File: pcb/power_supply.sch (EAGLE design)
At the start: 19 parts, among them J1 10103594-0001LF, U1 RASPBERRY_PI_3_MODEL_B+, U2 LM1085IT-5.0, U3 TI_NATIONAL_SEMICONDUCTOR_LM2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, X1 MKKDS02, X2 MKKDS02, X3 MKKDS02, X4 MKKDS02

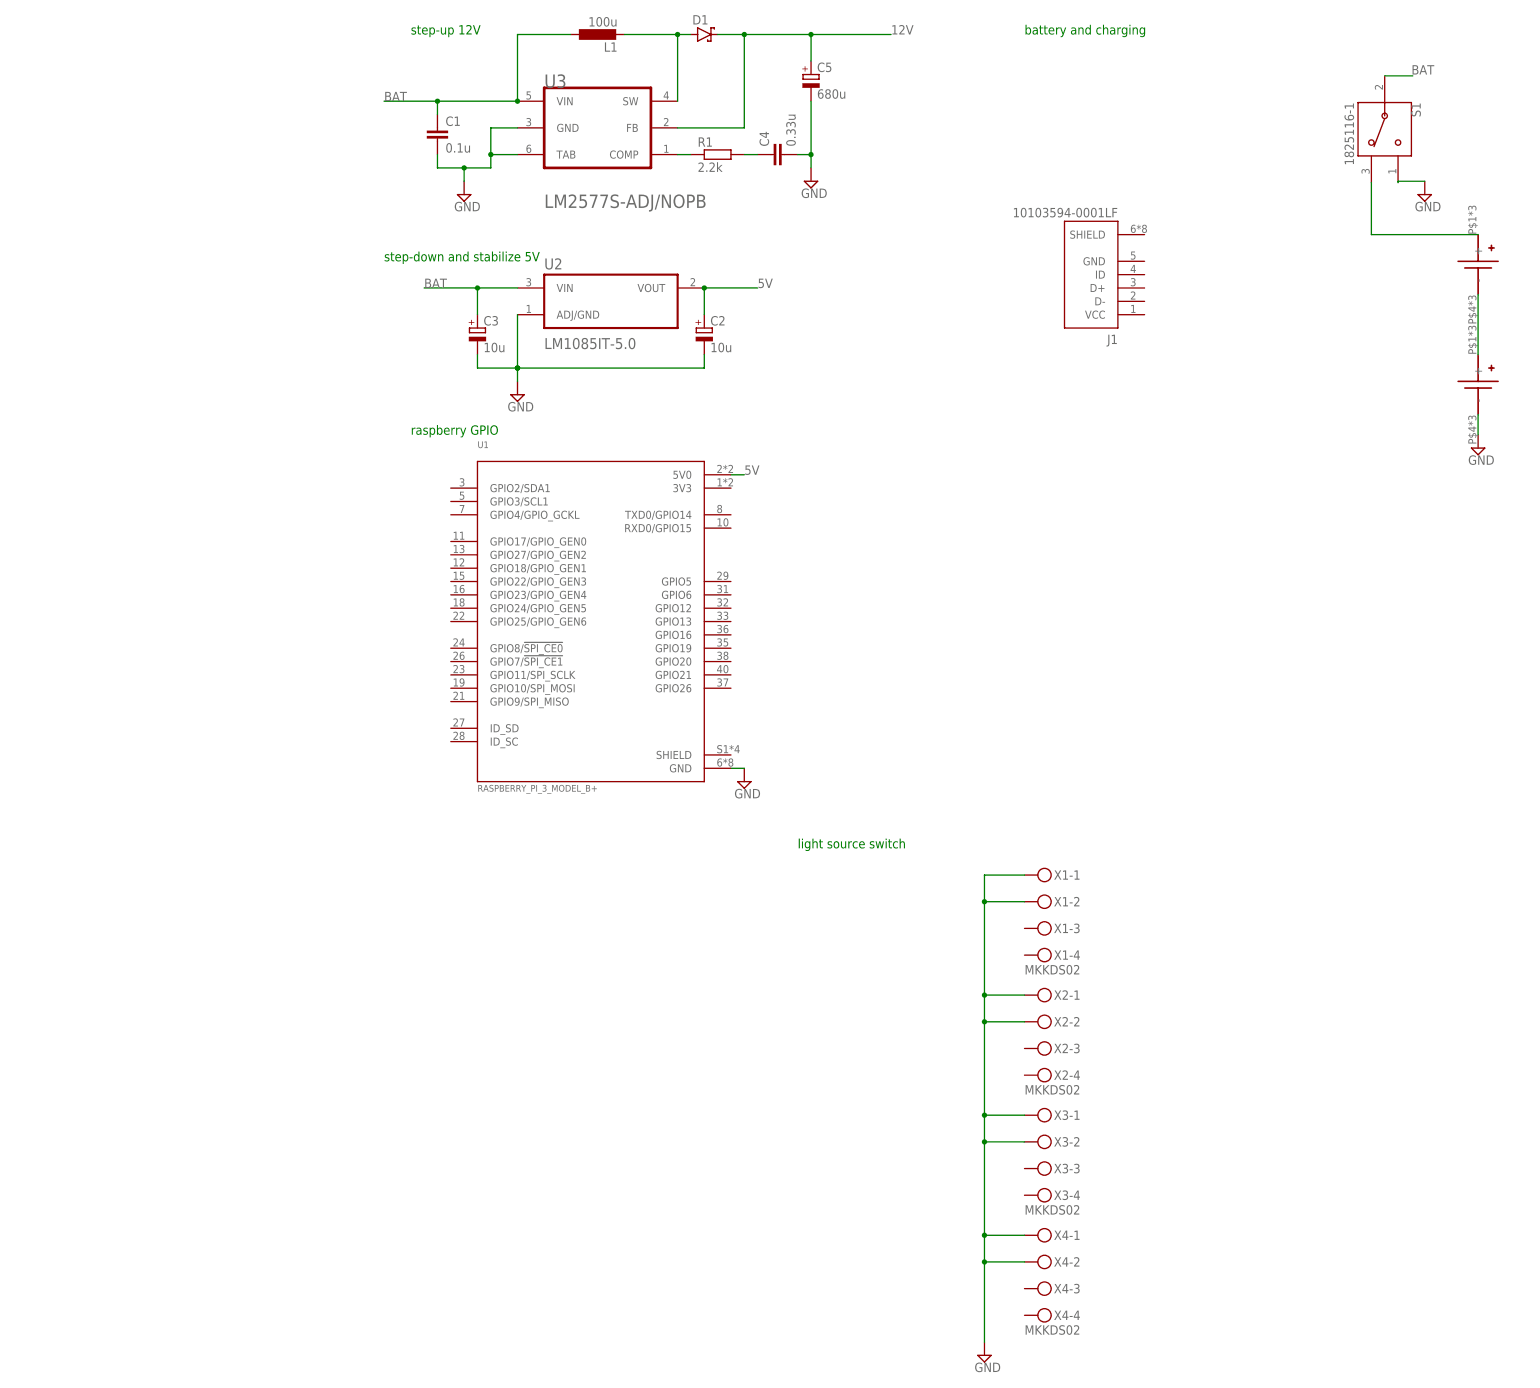
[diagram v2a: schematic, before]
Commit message: pcb - lights switching, battery replacement to 2*6V
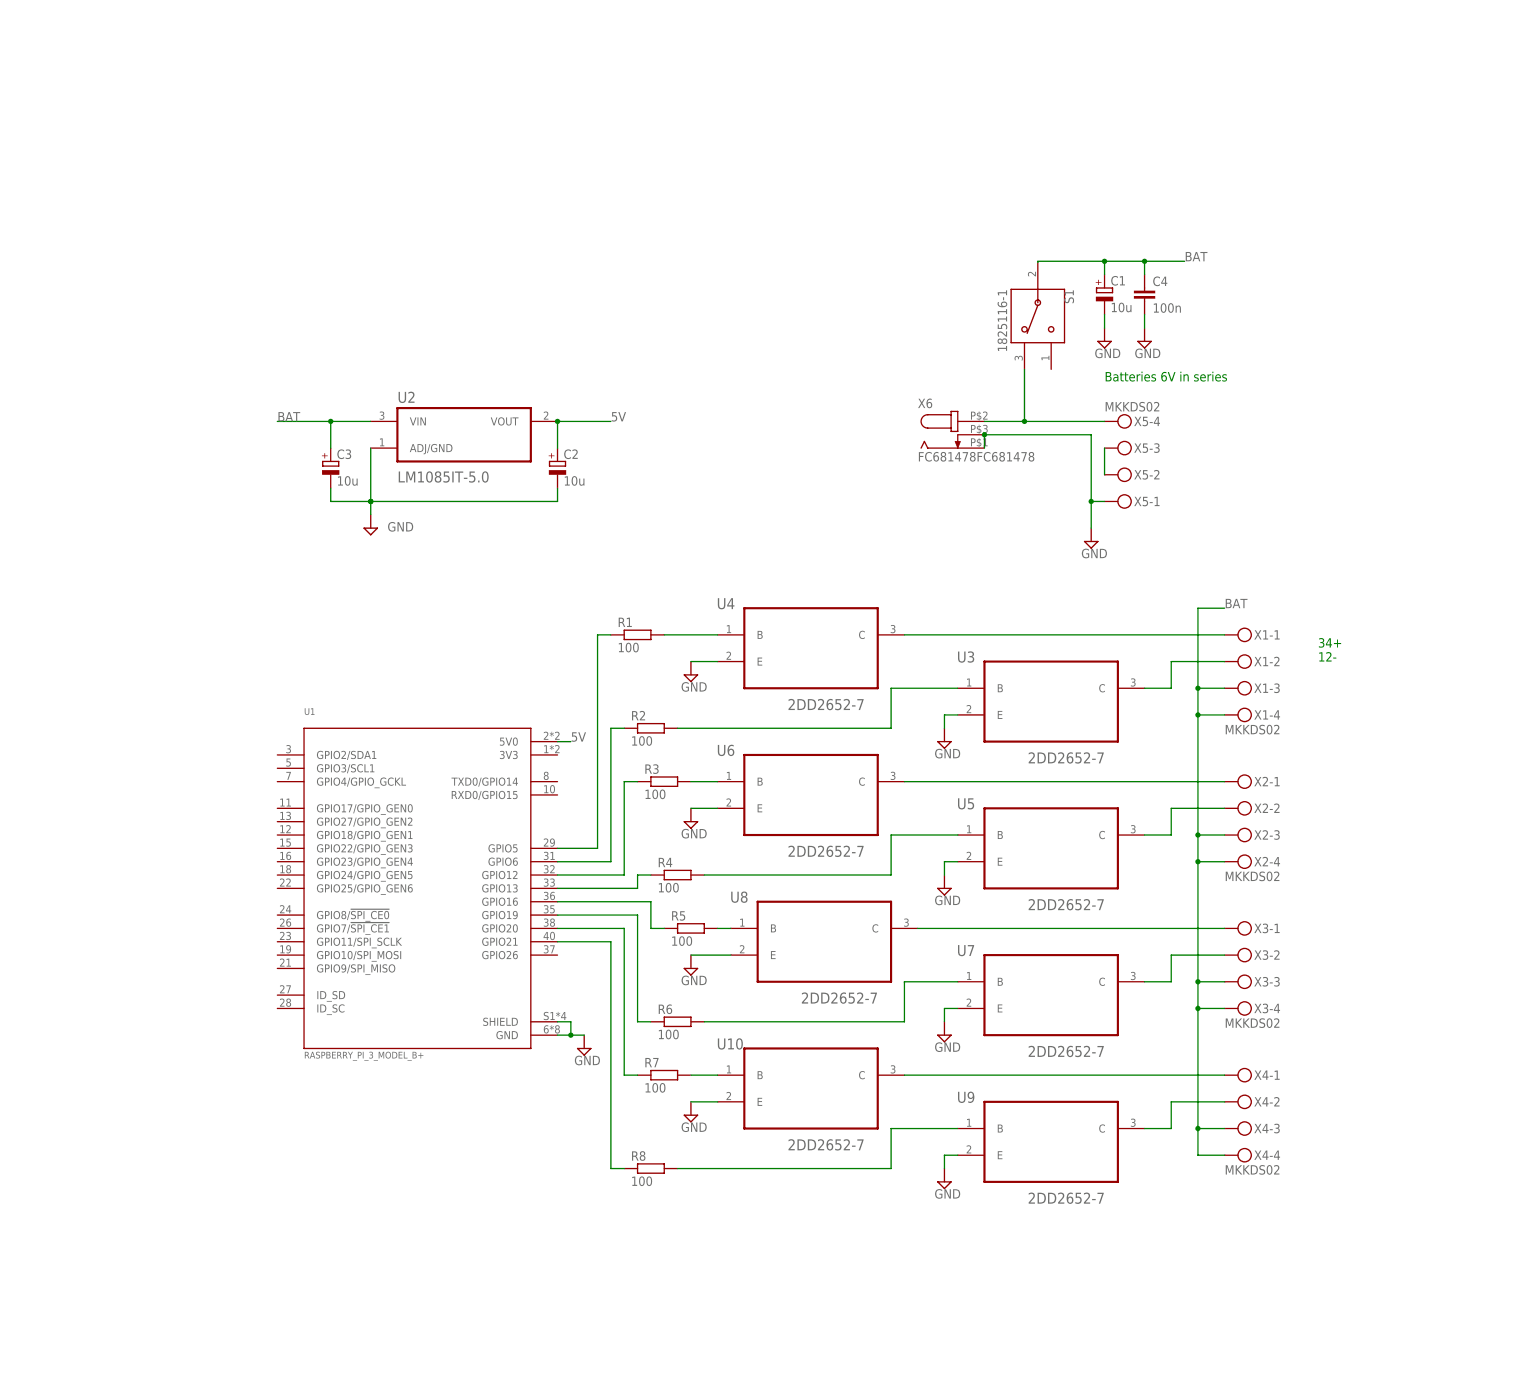
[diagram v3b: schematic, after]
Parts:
- removed C5: 680u, rcl:CPOL-EUSMCB
- removed D1: (no value), diode:SCHOTTKY-DIODEDO35-7
- removed J1: 10103594-0001LF, 10103594-0001LF:10103594-0001LF
- removed L1: 100u, rcl:L-EU0207/5V
- removed U$1, U$2: KEYESTONE_54A_3D, battery-holders:KEYESTONE_54A_3D
- added R2, R3, R4, R5, R6, R7, R8: 100, rcl:R-EU_R0805
- added U10, U4, U5, U6, U7, U8, U9: 2DD2652-7, 2DD2652-7:2DD2652-7
- added X5: MKKDS02, con-phoenix-508:MKKDS02
- added X6: FC681478FC681478, FC681478:FC681478FC681478
- C1: value 0.1u -> 10u; device rcl:C-EUC0805 -> rcl:CPOL-EUSMCB
- C4: value 0.33u -> 100n
- R1: value 2.2k -> 100
- U3: value TI_NATIONAL_SEMICONDUCTOR_LM2577S-ADJ-NOPBTI_NATIONAL_SEMICONDUCTOR_LM2577S-ADJ-NOPB_0_2 -> 2DD2652-7; device LM2577S-ADJ_NOPB:TI_NATIONAL_SEMICONDUCTOR_LM2577S-ADJ-NOPBTI_NATIONAL_SEMICONDUCTOR_LM2577S-ADJ-NOPB_0_2 -> 2DD2652-7:2DD2652-7
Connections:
- removed net 12V: C5.+, D1.C, U3.FB
- new net N$10: U6.C, X2-1.KL
- new net N$11: R4.2, U5.B
- new net N$12: U8.C, X3-1.KL
- new net N$13: U10.C, X4-1.KL
- new net N$14: U5.C, X2-2.KL
- new net N$15: U7.C, X3-2.KL
- new net N$16: U9.C, X4-2.KL
- new net N$17: R3.1, U1.GPIO12
- new net N$18: R7.1, U1.GPIO20
- new net N$19: R5.1, U1.GPIO16
- new net N$20: R6.2, U7.B
- new net N$21: R2.1, U1.GPIO6
- new net N$22: R1.2, U4.B
- new net N$23: R4.1, U1.GPIO13
- new net N$24: R3.2, U6.B
- new net N$25: R8.2, U9.B
- new net N$26: R5.2, U8.B
- new net N$27: R7.2, U10.B
- new net N$6: R2.2, U3.B
- new net N$8: U3.C, X1-2.KL
- new net N$9: R8.1, U1.GPIO21
- net BAT: now also C1.+, C4.1, X1-3.KL, X1-4.KL, X2-3.KL, X2-4.KL, X3-3.KL, X3-4.KL, X4-3.KL, X4-4.KL; no longer C1.1, L1.1, U3.VIN
- net GND: now also C1.-, U1.SHIELD, U10.E, U3.E, U4.E, U5.E, U6.E, U7.E, U8.E, U9.E, X5-1.KL, X6.1, X6.2; no longer C1.2, C5.-, S1.1, U$2.-, U3.GND, U3.TAB, X1-1.KL, X1-2.KL, X2-1.KL, X2-2.KL, X3-1.KL, X3-2.KL, X4-1.KL, X4-2.KL
- net N$1: now also U4.C, X1-1.KL; no longer U$1.-, U$2.+
- net N$3: now also X5-4.KL, X6.3; no longer U$1.+
- net N$4: now also X5-2.KL, X5-3.KL; no longer R1.1, U3.COMP
- net N$5: now also R1.1, U1.GPIO5; no longer D1.A, L1.2, U3.SW
- net N$7: now also R6.1, U1.GPIO19; no longer C4.1, R1.2
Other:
- note added: "34+ 12-"
- note added: "Batteries 6V in series"
- note removed: "battery and charging"
- note removed: "light source switch"
- note removed: "raspberry GPIO"
- note removed: "step-down and stabilize 5V"
- note removed: "step-up 12V"
- moved on the sheet: C2, C3, C4, R1, S1, U1, U2, X1-1, X1-2, X1-3, X1-4, X2-1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

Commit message: Some battery replacement and stuff
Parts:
- removed C3: 10u, rcl:CPOL-EUSMCB
- removed S1: 1825116-1, 1825116-1:1825116-1
- added C5, C6, C7: 10u, rcl:CPOL-EUB/3528-21R
- added R9: (no value), pot:TRIM_EU-CA6V
- added U11: TI_NATIONAL_SEMICONDUCTOR_LM1085IT-12-NOPBTI_NATIONAL_SEMIC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, LM1085IT-12:TI_NATIONAL_SEMICONDUCTOR_LM1085IT-12-NOPBTI_NATIONAL_SEMICONDUCTOR_LM1085IT-12-NOPB_0_0
- added X7: MKDSN1,5/2-5,08, con-phoenix-508:MKDSN1,5/2-5,08
- C1, C2: device rcl:CPOL-EUSMCB -> rcl:CPOL-EUB/3528-21R
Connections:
- new net 12V: C2.+, R9.A, U11.OUT
- new net LIGHTS+: R9.S, X1-3.KL, X1-4.KL, X2-3.KL, X2-4.KL, X3-3.KL, X3-4.KL, X4-3.KL, X4-4.KL
- new net N$28: X7-1.KL
- net 5V: now also C5.+; no longer C2.+
- net BAT: now also C6.+, C7.+, U11.IN, X7-2.KL; no longer C3.+, S1.2, X1-3.KL, X1-4.KL, X2-3.KL, X2-4.KL, X3-3.KL, X3-4.KL, X4-3.KL, X4-4.KL
- net GND: now also C5.-, C6.-, C7.-, U11.GND; no longer C3.-
- net N$3: no longer S1.3
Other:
- note added: "switch"
- moved on the sheet: C1, C2

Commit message: pcb - schematic done for now
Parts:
- removed C5, C6, C7: 10u, rcl:CPOL-EUB/3528-21R
- removed U1: RASPBERRY_PI_3_MODEL_B+, RASPBERRY_PI_3_MODEL_B_:RASPBERRY_PI_3_MODEL_B+
- removed U10, U3, U4, U5, U6, U7, U8, U9: 2DD2652-7, 2DD2652-7:2DD2652-7
- removed U11: TI_NATIONAL_SEMICONDUCTOR_LM1085IT-12-NOPBTI_NATIONAL_SEMIC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, LM1085IT-12:TI_NATIONAL_SEMICONDUCTOR_LM1085IT-12-NOPBTI_NATIONAL_SEMICONDUCTOR_LM1085IT-12-NOPB_0_0
- removed U2: LM1085IT-5.0, LM1085IT-5.0:LM1085IT-5.0
- removed X1, X2, X3, X4, X5: MKKDS02, con-phoenix-508:MKKDS02
- removed X6: FC681478FC681478, FC681478:FC681478FC681478
- removed X7: MKDSN1,5/2-5,08, con-phoenix-508:MKDSN1,5/2-5,08
- added BATTERY1, BATTERY2, SWITCH1: 1751248, con-phoenix-350:1751248
- added C3: 10u, rcl:CPOL-EUB/3528-21R
- added DC_CON: FC681478FC681478, FC681478:FC681478FC681478
- added L1, L2, L3, L4, L5, L6, L7, L8: (no value), con-phoenix-254:MPT2
- added LM1085IT-ADJ_1, LM1085IT-ADJ_2: LM1085IT-ADJ, LM1085IT-ADJ:LM1085IT-ADJ
- added P1: 2k, pot:TRIM_EU-CA6V
- added Q1, Q2, Q3, Q4, Q5, Q6, Q7, Q8: DIODES_FMMT493ATADIODES_FMMT493ATA_0_0, Diodes - FMMT493ATA:DIODES_FMMT493ATADIODES_FMMT493ATA_0_0
- added R10, R12: 120, rcl:R-EU_R0805
- added R11: 200, rcl:R-EU_R0805
- added R13: 39, rcl:R-EU_R0805
- added R14: 10, rcl:R-EU_R0805
- added RASPBERRY: RASPBERRY_PI_3_MODEL_B+, RASPBERRY_PI_3_MODEL_B_:RASPBERRY_PI_3_MODEL_B+
- C4: value 100n -> 10u; device rcl:C-EUC0805 -> rcl:CPOL-EUB/3528-21R
- R9: value (none) -> 120; device pot:TRIM_EU-CA6V -> rcl:R-EU_R0805
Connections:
- removed net 12V: C2.+, R9.A, U11.OUT
- removed net N$28: X7-1.KL
- new net N$2: LM1085IT-ADJ_2.ADJ/GND, R10.1, R11.2
- new net N$29: LM1085IT-ADJ_1.ADJ/GND, P1.S, R9.1
- new net N$30: R11.1, R12.2
- new net N$31: R12.1, R13.2
- new net N$32: R13.1, R14.1
- net 5V: now also C4.+, LM1085IT-ADJ_2.OUT, R10.2, RASPBERRY.5V0; no longer C5.+, U1.5V0, U2.VOUT
- net BAT: now also C3.+, LM1085IT-ADJ_1.IN, LM1085IT-ADJ_2.IN, SWITCH1-2.K; no longer C4.1, C6.+, C7.+, U11.IN, U2.VIN, X7-2.KL
- net GND: now also BATTERY2-2.K, C3.-, C4.-, DC_CON.1, DC_CON.2, P1.A, Q1.E, Q2.E, Q3.E, Q4.E, Q5.E, Q6.E, Q7.E, Q8.E, R14.2, RASPBERRY.GND, RASPBERRY.SHIELD; no longer C4.2, C5.-, C6.-, C7.-, U1.GND, U1.SHIELD, U10.E, U11.GND, U2.ADJ/GND, U3.E, U4.E, U5.E, U6.E, U7.E, U8.E, U9.E, X5-1.KL, X6.1, X6.2
- net LIGHTS+: now also C2.+, L1-1.1, L2-1.1, L3-1.1, L4-1.1, L5-1.1, L6-1.1, L7-1.1, L8-1.1, LM1085IT-ADJ_1.OUT, R9.2; no longer R9.S, X1-3.KL, X1-4.KL, X2-3.KL, X2-4.KL, X3-3.KL, X3-4.KL, X4-3.KL, X4-4.KL
- net N$1: now also L1-2.1, Q1.C; no longer U4.C, X1-1.KL
- net N$10: now also L4-2.1, Q4.C; no longer U6.C, X2-1.KL
- net N$11: now also Q5.B, R5.2; no longer R4.2, U5.B
- net N$12: now also L5-2.1, Q5.C; no longer U8.C, X3-1.KL
- net N$13: now also Q6.B, R6.2; no longer U10.C, X4-1.KL
- net N$14: now also L6-2.1, Q6.C; no longer U5.C, X2-2.KL
- net N$15: now also Q7.B, R7.2; no longer U7.C, X3-2.KL
- net N$16: now also L7-2.1, Q7.C; no longer U9.C, X4-2.KL
- net N$17: now also Q8.B, R8.2; no longer R3.1, U1.GPIO12
- net N$18: now also L8-2.1, Q8.C; no longer R7.1, U1.GPIO20
- net N$19: now also R1.1, RASPBERRY.GPIO5; no longer R5.1, U1.GPIO16
- net N$20: now also R2.1, RASPBERRY.GPIO6; no longer R6.2, U7.B
- net N$21: now also R3.1, RASPBERRY.GPIO12; no longer R2.1, U1.GPIO6
- net N$22: now also Q1.B; no longer U4.B
- net N$23: now also RASPBERRY.GPIO13; no longer U1.GPIO13
- net N$24: now also R5.1, RASPBERRY.GPIO16; no longer R3.2, U6.B
- net N$25: now also R6.1, RASPBERRY.GPIO19; no longer R8.2, U9.B
- net N$26: now also R7.1, RASPBERRY.GPIO20; no longer R5.2, U8.B
- net N$27: now also R8.1, RASPBERRY.GPIO21; no longer R7.2, U10.B
- net N$3: now also BATTERY1-1.K, DC_CON.3, SWITCH1-1.K; no longer X5-4.KL, X6.3
- net N$4: now also BATTERY1-2.K, BATTERY2-1.K; no longer X5-2.KL, X5-3.KL
- net N$5: now also Q2.B, R2.2; no longer R1.1, U1.GPIO5
- net N$6: now also L2-2.1, Q2.C; no longer R2.2, U3.B
- net N$7: now also Q3.B, R3.2; no longer R6.1, U1.GPIO19
- net N$8: now also L3-2.1, Q3.C; no longer U3.C, X1-2.KL
- net N$9: now also Q4.B, R4.2; no longer R8.1, U1.GPIO21
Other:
- note removed: "34+ 12-"
- note removed: "Batteries 6V in series"
- note removed: "switch"
- moved on the sheet: C1, C2, R1, R2, R3, R4, R5, R6, R7, R8

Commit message: pcb - board
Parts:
- removed BATTERY1, BATTERY2, SWITCH1: 1751248, con-phoenix-350:1751248
- removed LM1085IT-ADJ_2: LM1085IT-ADJ, LM1085IT-ADJ:LM1085IT-ADJ
- removed R13: 39, rcl:R-EU_R0805
- removed R14: 10, rcl:R-EU_R0805
- added ACC1, ACC2, SWITCH: 1751248, con-phoenix-350:1751248
- added U2: LM1085IT-ADJ, LM1085IT-ADJ:LM1085IT-ADJ
- DC_CON: value FC681478FC681478 -> FC681478WURTH_694106301002; device FC681478:FC681478FC681478 -> FC681478:FC681478WURTH_694106301002
- L1: value (none) -> 1
- R11: value 200 -> 330
- R12: value 120 -> 39
- renumbered LM1085IT-ADJ_1 to U1
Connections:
- removed net N$32: R13.1, R14.1
- net 5V: now also U2.OUT; no longer LM1085IT-ADJ_2.OUT
- net BAT: now also SWITCH-1.K, U2.IN; no longer LM1085IT-ADJ_2.IN, SWITCH1-2.K
- net GND: now also R12.1; no longer BATTERY2-2.K, DC_CON.2, R14.2
- net LIGHTS+: now also L1-2.1, L2-2.1, L3-2.1, L4-2.1, L5-2.1, L6-2.1, L7-2.1, L8-2.1; no longer L1-1.1, L2-1.1, L3-1.1, L4-1.1, L5-1.1, L6-1.1, L7-1.1, L8-1.1
- net N$1: now also L1-1.1; no longer L1-2.1
- net N$10: now also L4-1.1; no longer L4-2.1
- net N$12: now also L5-1.1; no longer L5-2.1
- net N$14: now also L6-1.1; no longer L6-2.1
- net N$16: now also L7-1.1; no longer L7-2.1
- net N$18: now also L8-1.1; no longer L8-2.1
- net N$2: now also U2.ADJ/GND; no longer LM1085IT-ADJ_2.ADJ/GND
- net N$3: now also ACC2-2.K, DC_CON.2; no longer BATTERY1-1.K, DC_CON.3, SWITCH1-1.K
- net N$31: now also ACC1-1.K, DC_CON.3, SWITCH-2.K; no longer R12.1, R13.2
- net N$4: now also ACC1-2.K, ACC2-1.K; no longer BATTERY1-2.K, BATTERY2-1.K
- net N$6: now also L2-1.1; no longer L2-2.1
- net N$8: now also L3-1.1; no longer L3-2.1
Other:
- moved on the sheet: C3, C4, DC_CON, R10, R11, R12
